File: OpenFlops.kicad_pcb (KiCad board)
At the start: 2 copper layers, 111.6 x 59.4 mm, 87 parts, among them P1 FLOPPY_CONN, P10 SD CARD, P11 SD PWR, P12 SD_DISABLE, P2 POWER_INPUT, P3 USB_A_FEMALE, P4 PROG_PORT, P5 JUMPER_JC, P6 ENCODER_PORT, P7 DISPLAY_PORT, P8 USB_HEADER, P9 EXTERNAL_SPEAKER, Q1 BSS138, Q2 BSS138, Q3 BSS138, Q5 BSS138, Q6 BSS138, Q7 MMBT3904, Q8 BSS138, U1 74HCT04, U3 STM32F105RBT6, U4 LM1117MP-3.3, Y1 8 MHz

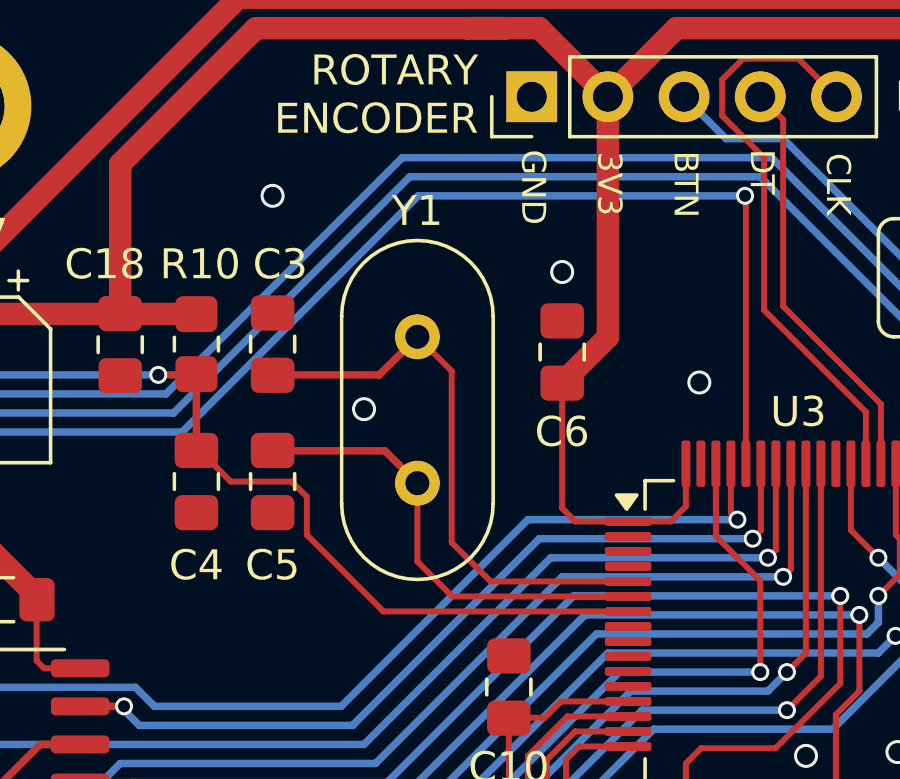
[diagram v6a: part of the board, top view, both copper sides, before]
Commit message: Switch crystal to SMD
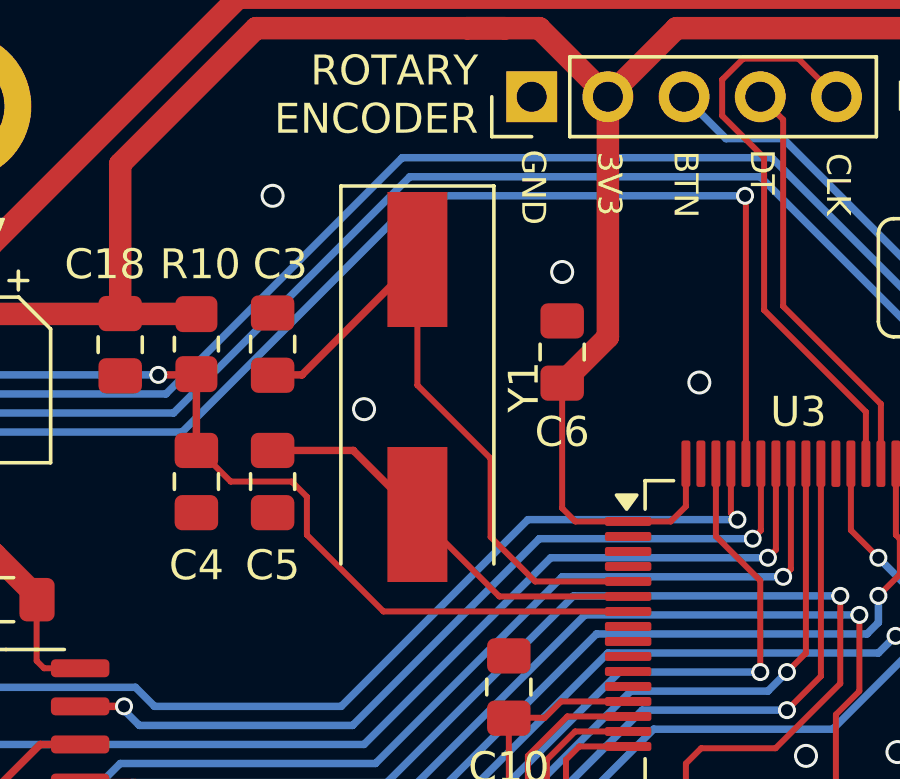
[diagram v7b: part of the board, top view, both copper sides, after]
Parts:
- Y1: footprint Crystal:Crystal_HC49-U_Vertical -> Crystal:Crystal_SMD_HC49-SD
- moved Y1 1.67 mm to (154.9, 70.0)
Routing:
- net Net-(U3-PD0): track 19.1 -> 21.9 mm
- net Net-(U3-PD1): track 15.4 -> 13.9 mm
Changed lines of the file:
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@@
 		)
 	)
-	(footprint "Crystal:Crystal_HC49-U_Vertical"
+	(footprint "Crystal:Crystal_SMD_HC49-SD"
 		(layer "F.Cu")
-		(at 154.94 68.326 -90)
-		(descr "Crystal THT HC-49/U http://5hertz.com/pdfs/04404_D.pdf")
-		(tags "THT crystalHC-49/U")
+		(at 154.94 70 -90)
+		(descr "SMD Crystal HC-49-SD http://cdn-reichelt.de/documents/datenblatt/B400/xxx-HC49-SMD.pdf, 11.4x4.7mm^2 package")
+		(tags "SMD SMT crystal")
 		(property "Reference" "Y1"
-			(at -4.191 0 180)
+			(at 0 -3.55 -90)
 			(layer "F.SilkS")
 			(effects
@@
 		)
 		(property "Value" "8 MHz"
-			(at 2.44 3.525 90)
+			(at 0 3.55 -90)
 			(layer "F.Fab")
 			(effects
@@
 			)
 		)
-		(property "Footprint" "Crystal:Crystal_HC49-U_Vertical"
+		(property "Footprint" "Crystal:Crystal_SMD_HC49-SD"
 			(at 0 0 -90)
+			(unlocked yes)
 			(layer "F.Fab")
 			(hide yes)
@@
 		(property "Datasheet" ""
 			(at 0 0 -90)
+			(unlocked yes)
 			(layer "F.Fab")
 			(hide yes)
@@
 		(property "Description" ""
 			(at 0 0 -90)
+			(unlocked yes)
 			(layer "F.Fab")
 			(hide yes)
@@
 		(sheetname "Root")
 		(sheetfile "OpenFlops.kicad_sch")
-		(attr through_hole)
+		(attr smd)
 		(fp_line
-			(start -0.685 2.525)
-			(end 5.565 2.525)
+			(start -6.7 2.55)
+			(end 5.9 2.55)
 			(stroke
 				(width 0.12)
@@
 		)
 		(fp_line
-			(start -0.685 -2.525)
-			(end 5.565 -2.525)
-			(stroke
-				(width 0.12)
-				(type solid)
-			)
-			(layer "F.SilkS")
-		)
-		(fp_arc
-			(start -0.685 2.525)
-			(mid -3.21 0)
-			(end -0.685 -2.525)
+			(start -6.7 -2.55)
+			(end -6.7 2.55)
 			(stroke
 				(width 0.12)
@@
 			(layer "F.SilkS")
 		)
-		(fp_arc
-			(start 5.565 -2.525)
-			(mid 8.09 0)
-			(end 5.565 2.525)
+		(fp_line
+			(start 5.9 -2.55)
+			(end -6.7 -2.55)
 			(stroke
 				(width 0.12)
@@
 		)
 		(fp_line
-			(start -3.5 2.8)
-			(end 8.4 2.8)
+			(start -6.8 2.6)
+			(end 6.8 2.6)
 			(stroke
 				(width 0.05)
@@
 		)
 		(fp_line
-			(start 8.4 2.8)
-			(end 8.4 -2.8)
+			(start 6.8 2.6)
+			(end 6.8 -2.6)
 			(stroke
 				(width 0.05)
@@
 		)
 		(fp_line
-			(start -3.5 -2.8)
-			(end -3.5 2.8)
+			(start -6.8 -2.6)
+			(end -6.8 2.6)
 			(stroke
 				(width 0.05)
@@
 		)
 		(fp_line
-			(start 8.4 -2.8)
-			(end -3.5 -2.8)
+			(start 6.8 -2.6)
+			(end -6.8 -2.6)
 			(stroke
 				(width 0.05)
@@
 		)
 		(fp_line
-			(start -0.685 2.325)
-			(end 5.565 2.325)
+			(start -5.7 2.35)
+			(end 5.7 2.35)
 			(stroke
 				(width 0.1)
@@
 		)
 		(fp_line
-			(start -0.56 2)
-			(end 5.44 2)
+			(start 5.7 2.35)
+			(end 5.7 -2.35)
 			(stroke
 				(width 0.1)
@@
 		)
 		(fp_line
-			(start -0.56 -2)
-			(end 5.44 -2)
+			(start -3.015 2.115)
+			(end 3.015 2.115)
 			(stroke
 				(width 0.1)
@@
 		)
 		(fp_line
-			(start -0.685 -2.325)
-			(end 5.565 -2.325)
+			(start -3.015 -2.115)
+			(end 3.015 -2.115)
 			(stroke
 				(width 0.1)
@@
 			(layer "F.Fab")
 		)
-		(fp_arc
-			(start -0.685 2.325)
-			(mid -3.01 0)
-			(end -0.685 -2.325)
+		(fp_line
+			(start -5.7 -2.35)
+			(end -5.7 2.35)
 			(stroke
 				(width 0.1)
@@
 			(layer "F.Fab")
 		)
-		(fp_arc
-			(start -0.56 2)
-			(mid -2.56 0)
-			(end -0.56 -2)
+		(fp_line
+			(start 5.7 -2.35)
+			(end -5.7 -2.35)
 			(stroke
 				(width 0.1)
@@
 		)
 		(fp_arc
-			(start 5.44 -2)
-			(mid 7.44 0)
-			(end 5.44 2)
+			(start -3.015 2.115)
+			(mid -5.13 0)
+			(end -3.015 -2.115)
 			(stroke
 				(width 0.1)
@@
 		)
 		(fp_arc
-			(start 5.565 -2.325)
-			(mid 7.89 0)
-			(end 5.565 2.325)
+			(start 3.015 -2.115)
+			(mid 5.13 0)
+			(end 3.015 2.115)
 			(stroke
 				(width 0.1)
@@
 		)
 		(fp_text user "${REFERENCE}"
-			(at 2.44 0 90)
+			(at 0 0 -90)
 			(layer "F.Fab")
 			(effects
@@
 			)
 		)
-		(pad "1" thru_hole circle
-			(at 0 0 270)
-			(size 1.5 1.5)
-			(drill 0.8)
-			(layers "*.Cu" "*.Mask")
-			(remove_unused_layers no)
+		(pad "1" smd rect
+			(at -4.25 0 270)
+			(size 4.5 2)
+			(layers "F.Cu" "F.Paste" "F.Mask")
 			(net 2 "Net-(U3-PD0)")
 			(pinfunction "1")
 			(pintype "passive")
 		)
-		(pad "2" thru_hole circle
-			(at 4.88 0 270)
-			(size 1.5 1.5)
-			(drill 0.8)
-			(layers "*.Cu" "*.Mask")
-			(remove_unused_layers no)
+		(pad "2" smd rect
+			(at 4.25 0 270)
+			(size 4.5 2)
+			(layers "F.Cu" "F.Paste" "F.Mask")
 			(net 4 "Net-(U3-PD1)")
 			(pinfunction "2")
 			(pintype "passive")
 		)
-		(model "${KISYS3DMOD}/Crystal.3dshapes/Crystal_HC49-U_Vertical.wrl"
+		(model "${KICAD8_3DMODEL_DIR}/Crystal.3dshapes/Crystal_SMD_HC49-SD.wrl"
 			(offset
 				(xyz 0 0 0)
 			)
 			(scale
-				(xyz 1 1 0.21)
+				(xyz 1 1 1)
 			)
 			(rotate
@@
 	)
 	(segment
-		(start 156.083 69.469)
-		(end 154.94 68.326)
+		(start 154.94 69.94)
+		(end 154.94 65.75)
 		(width 0.2)
 		(layer "F.Cu")
@@
 	)
 	(segment
-		(start 150.114 69.596)
-		(end 153.67 69.596)
-		(width 0.25)
+		(start 157.381 75)
+		(end 157.381 72.381)
+		(width 0.2)
+		(layer "F.Cu")
+		(net 2)
+	)
+	(segment
+		(start 157.381 72.381)
+		(end 154.94 69.94)
+		(width 0.2)
 		(layer "F.Cu")
 		(net 2)
 	)
 	(segment
-		(start 157.381 76.482)
-		(end 156.083 75.184)
+		(start 158.863 76.482)
+		(end 157.381 75)
 		(width 0.2)
 		(layer "F.Cu")
@@
 	(segment
 		(start 161.965 76.482)
-		(end 157.381 76.482)
+		(end 158.863 76.482)
 		(width 0.2)
 		(layer "F.Cu")
@@
 	)
 	(segment
-		(start 153.67 69.596)
-		(end 154.94 68.326)
+		(start 151.094 69.596)
+		(end 154.94 65.75)
 		(width 0.25)
 		(layer "F.Cu")
@@
 	)
 	(segment
-		(start 156.083 75.184)
-		(end 156.083 69.469)
-		(width 0.2)
+		(start 150.114 69.596)
+		(end 151.094 69.596)
+		(width 0.25)
 		(layer "F.Cu")
 		(net 2)
@@
 	)
 	(segment
-		(start 156.103 76.982)
-		(end 161.965 76.982)
+		(start 154.94 74.25)
+		(end 157.672 76.982)
 		(width 0.2)
 		(layer "F.Cu")
@@
 	)
 	(segment
-		(start 153.861 72.127)
-		(end 154.94 73.206)
-		(width 0.25)
-		(layer "F.Cu")
-		(net 4)
-	)
-	(segment
-		(start 154.94 75.819)
-		(end 156.103 76.982)
+		(start 157.672 76.982)
+		(end 161.965 76.982)
 		(width 0.2)
 		(layer "F.Cu")
@@
 	)
 	(segment
-		(start 150.114 72.127)
-		(end 153.861 72.127)
+		(start 150.114 72.1145)
+		(end 152.8045 72.1145)
 		(width 0.25)
 		(layer "F.Cu")
@@
 	)
 	(segment
-		(start 154.94 73.206)
-		(end 154.94 75.819)
-		(width 0.2)
+		(start 152.8045 72.1145)
+		(end 154.94 74.25)
+		(width 0.25)
 		(layer "F.Cu")
 		(net 4)

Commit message: Final touches
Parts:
- P4: footprint Connector_PinHeader_2.54mm:PinHeader_2x05_P2.54mm_Vertical -> Connector_PinHeader_2.54mm:PinHeader_2x06_P2.54mm_Vertical
- moved V0 20.2 mm to (188.3, 79.0)
- moved C7 4.82 mm to (183.4, 75.5), turned to -90 degrees
- moved P5 2.55 mm to (108.1, 76.2), turned to -90 degrees
- moved P4 2.54 mm to (108.1, 72.1)
- moved R20 1.85 mm to (191.0, 66.5)
- moved R21 1.75 mm to (191.0, 69.1)
- moved C4 0.66 mm to (147.6, 73.8)
- moved C5 0.66 mm to (150.1, 73.8)
- turned R6 to 180 degrees
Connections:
- P4 pad 10: +3.3V -> GND
- P4 pad 3: /rx -> /swdio
- P4 pad 4: +5V -> /swclk
- P4 pad 5: /tx -> /rx
- P4 pad 6: GND -> +5V
- P4 pad 7: +3.3V -> /tx
- P4 pad 9: /boot0 -> +3.3V
- S3 pad 1: GND -> Net-(U3-PC7)
- S3 pad 2: Net-(U3-PC7) -> GND
- U3 pad 46: unconnected-(U3-PA13-Pad46) -> /swdio
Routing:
- net /swdio: track 0.00 -> 79.2 mm, vias 0 -> 1
- net /swclk: track 0.00 -> 73.5 mm, vias 0 -> 1
- net /~{index}: track 26.7 -> 45.0 mm
- net /~{rdy}: track 43.2 -> 58.5 mm
- net Net-(U3-PC7): track 50.8 -> 41.6 mm
- net Net-(U3-PC8): track 43.2 -> 39.2 mm
- net +3.3V: track 264.1 -> 260.3 mm
- net /spi_cs: track 18.0 -> 14.7 mm
- net /spk+: track 16.6 -> 13.4 mm
- net /spi_clk: track 20.5 -> 17.8 mm
- net /~{dskchg}: track 59.2 -> 56.5 mm
- net /spi_do: track 20.3 -> 18.5 mm
- net /tx: track 88.6 -> 87.2 mm
- net /~{side}: track 112.0 -> 113.3 mm
- net /rx: track 84.6 -> 83.4 mm
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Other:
- board text added: "RST"
- board text added: "SWCLK"
- board text added: "SWDIO"
- board text removed: "RESET"
